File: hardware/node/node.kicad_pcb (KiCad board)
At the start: 4 copper layers, 48.5 x 50 mm, 68 parts, among them J1 BOOT0_Jumper, J2 FTDI, J3 SMA Female, J4 2 x AA, J5 SWD, Q1 Si2323DDS, SW1 DTSM-65R-V-B, U1 RFM69HW, U2 SHTC3, U3 AT25DF512C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

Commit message: Further cleanup of node PCB
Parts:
- moved C5 1.60 mm to (93.5, 75.5), turned to 90 degrees
- moved R32 1.24 mm to (96.4, 89.0), turned to 180 degrees
- moved C6 0.25 mm to (82.8, 90.3)
- moved U3 0.25 mm to (79.0, 88.5)
- turned R18 to 0 degrees
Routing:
- net VCC: track 51.1 -> 55.8 mm, vias 14 -> 16
- net GND: track 124.8 -> 127.4 mm, vias 17 -> 19
- net /V_BAT_MID: track 7.14 -> 4.66 mm
- net /LEDG: track 25.8 -> 24.8 mm

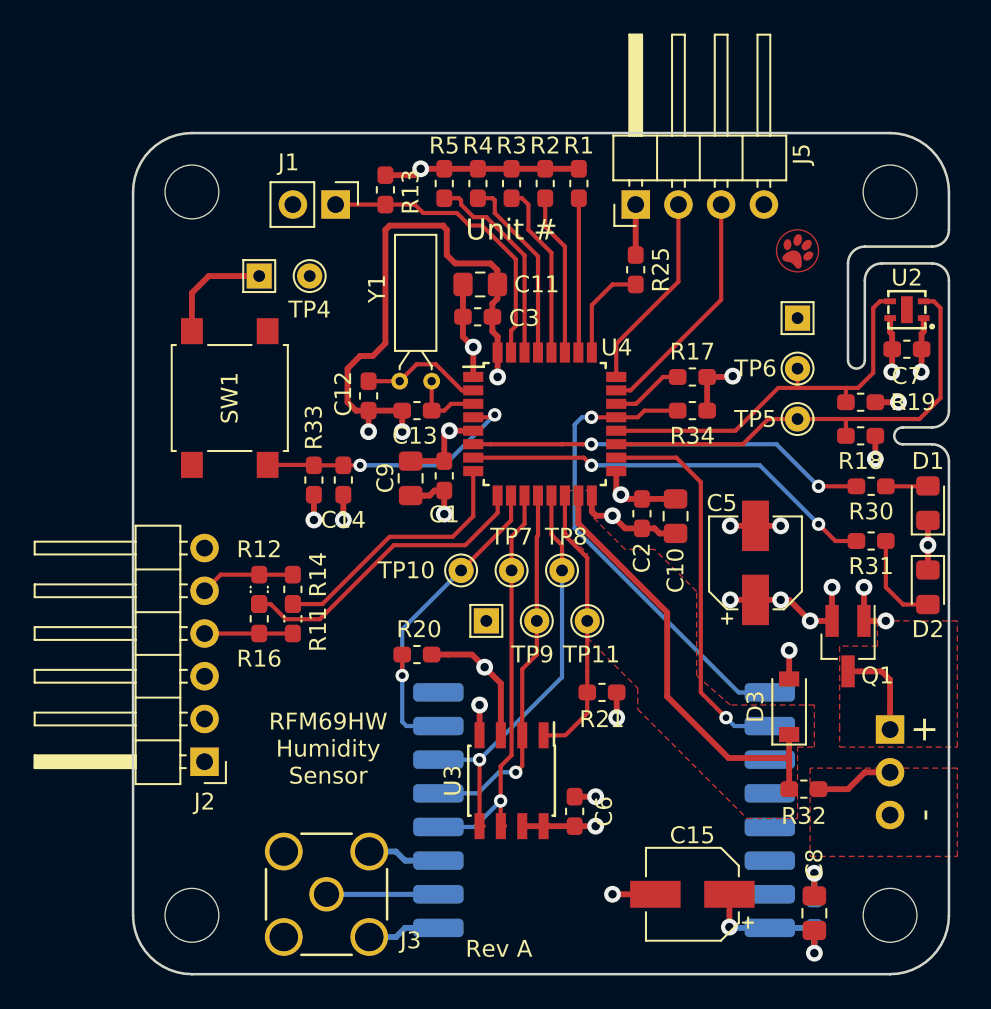
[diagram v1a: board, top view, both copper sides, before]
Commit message: Added an extra push button for user input
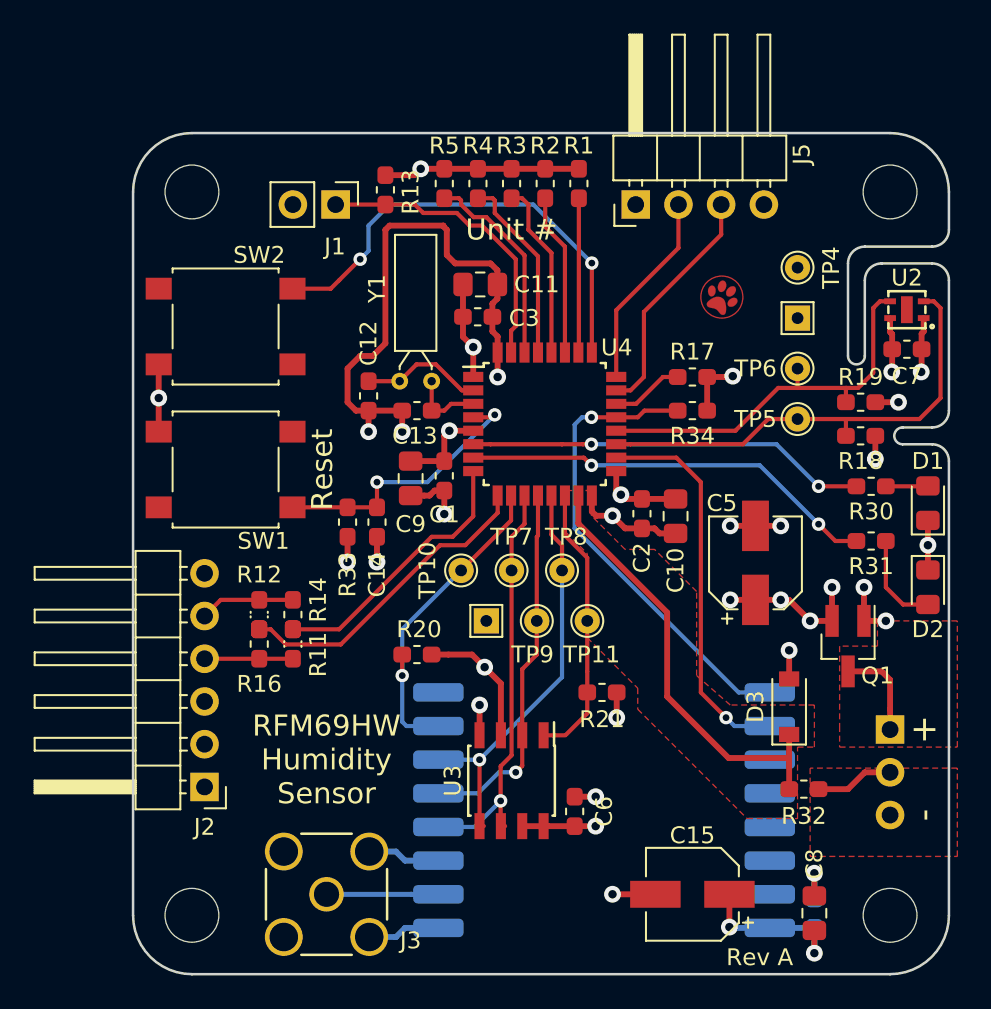
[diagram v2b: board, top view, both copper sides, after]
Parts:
- removed R25: 100k, Resistor_SMD:R_0603_1608Metric_Pad1.05x0.95mm_HandSolder
- removed TP2: TestPoint, TestPoint:TestPoint_THTPad_1.5x1.5mm_Drill0.7mm
- added SW2: DTSM-65R-V-B, humidity:SW_SPST_DTSM-6, F.Cu at (62.0, 61.5)
- moved TP4 29.0 mm to (96.0, 58.0)
- moved G*** 5.27 mm to (91.5, 59.8)
- moved SW1 4.26 mm to (62.0, 70.0), turned to 180 degrees
- moved G*** 3.50 mm to (65.0, 64.0)
- moved C14 3.20 mm to (71.0, 73.1)
- moved R33 3.20 mm to (69.2, 73.1)
- moved J2 1.50 mm to (60.8, 88.9)
- moved R11 1.50 mm to (66.0, 80.4)
- moved R12 1.50 mm to (64.0, 78.6)
- moved R14 1.50 mm to (66.0, 78.6)
- moved R16 1.50 mm to (64.0, 80.4)
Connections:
- SW1 pad 1: Net-(SW1-Pad1) -> /STM_RESET
- SW1 pad 2: /STM_RESET -> Net-(SW1-Pad2)
- SW1 pad 3: GND -> Net-(SW1-Pad3)
- SW1 pad 4: Net-(SW1-Pad4) -> GND
- U4 pad 25: /PA15 -> /SW
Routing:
- net /SW: track 0.00 -> 27.5 mm, vias 0 -> 2
- net /PA15: track 5.93 -> 0.00 mm
- net GND: track 127.4 -> 121.7 mm, vias 19 -> 20
- net /USART2_TX: track 15.6 -> 16.2 mm
- net /USART2_RX: track 18.2 -> 18.8 mm
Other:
- outline, holes or cut-outs redrawn
- board text added: "CLK"
- board text added: "IO"
- board text added: "OOS 2019-08-07"
- board text added: "Reset"
- board text added: "SWD"
- board text removed: "OOS 2019-06-25"
- board text removed: "SWCLK"
- board text removed: "SWDIO"

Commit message: Added pulldown to switch
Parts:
- added R6: 100k, Resistor_SMD:R_0603_1608Metric_Pad1.05x0.95mm_HandSolder, F.Cu at (68.0, 61.2)
- turned SW2 to 180 degrees
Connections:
- SW2 pad 1: Net-(SW2-Pad1) -> /SW
- SW2 pad 2: /SW -> Net-(SW2-Pad2)
- SW2 pad 3: GND -> Net-(SW2-Pad3)
- SW2 pad 4: Net-(SW2-Pad4) -> VCC
- U4 pad 25: /SW -> /LEDR
- U4 pad 6: /LEDR -> /SW
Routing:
- net /SW: track 27.5 -> 22.5 mm
- net /LEDR: track 23.8 -> 19.9 mm
- net VCC: track 55.8 -> 57.3 mm, vias 16 -> 17
- net GND: track 121.7 -> 120.6 mm, vias 20 -> 21

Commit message: Updated date
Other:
- board text added: "OOS 2019-08-25"
- board text removed: "OOS 2019-08-07"
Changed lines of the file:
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@@
   )
   (setup
-    (last_trace_width 0.29337)
+    (last_trace_width 0.25)
     (user_trace_width 0.25)
     (user_trace_width 0.29337)
@@
     (pcbplotparams
       (layerselection 0x010fc_ffffffff)
-      (usegerberextensions false)
+      (usegerberextensions true)
       (usegerberattributes false)
       (usegerberadvancedattributes false)
@@
       (psa4output false)
       (plotreference true)
-      (plotvalue true)
+      (plotvalue false)
       (plotinvisibletext false)
       (padsonsilk false)
@@
       (outputformat 1)
       (mirror false)
-      (drillshape 1)
+      (drillshape 0)
       (scaleselection 1)
-      (outputdirectory ""))
+      (outputdirectory "gerbers/"))
   )
   (net 0 "")
@@
     (effects (font (size 1.5 1.5) (thickness 0.3)) (justify mirror))
   )
-  (gr_text "OOS 2019-08-07" (at 57.75 72.25 270) (layer B.SilkS)
+  (gr_text "OOS 2019-08-25" (at 57.75 72.25 270) (layer B.SilkS)
     (effects (font (size 1 1) (thickness 0.2)) (justify left mirror))
   )

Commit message: Add silkscreen for JLCPCB order number
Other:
- board text added: "JLCJLCJLCJLC"
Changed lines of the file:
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@@
   (general
     (thickness 1.6)
-    (drawings 54)
+    (drawings 55)
     (tracks 395)
     (zones 0)
@@
     )
   )
+  (gr_text JLCJLCJLCJLC (at 91.25 90.75 90) (layer B.SilkS)
+    (effects (font (size 1 1) (thickness 0.2)) (justify mirror))
+  )
   (gr_text VCC (at 94 50.1 90) (layer B.SilkS)
